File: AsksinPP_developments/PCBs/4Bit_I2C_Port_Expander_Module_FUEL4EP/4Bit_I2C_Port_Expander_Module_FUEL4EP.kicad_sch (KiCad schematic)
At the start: 22 parts, among them J1 Conn_01x04, J2 Conn_01x04, J3 Conn_01x04, J4 Conn_01x04, Q1 2N7000, Q2 2N7000, Q3 2N7000, Q4 2N7000, U1 PCA9536D

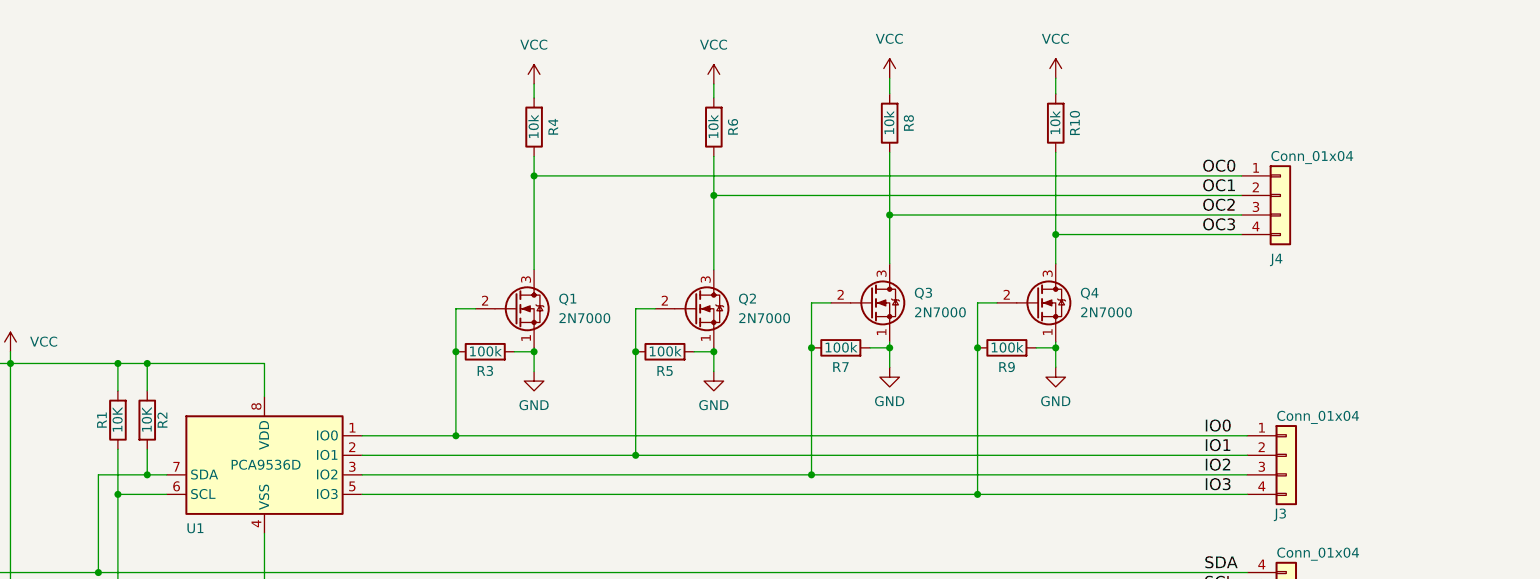
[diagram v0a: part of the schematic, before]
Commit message: PCB: I2C_Module_SHT85_BME280_FUEL4EP, I2C_Module_BME680_FUEL4EP: correction of connector placements in 3D view; 4Bit_I2C_Port_Expander_Module_FUEL4EP: change from 2N7000 to 2N7002K for SMD assembly
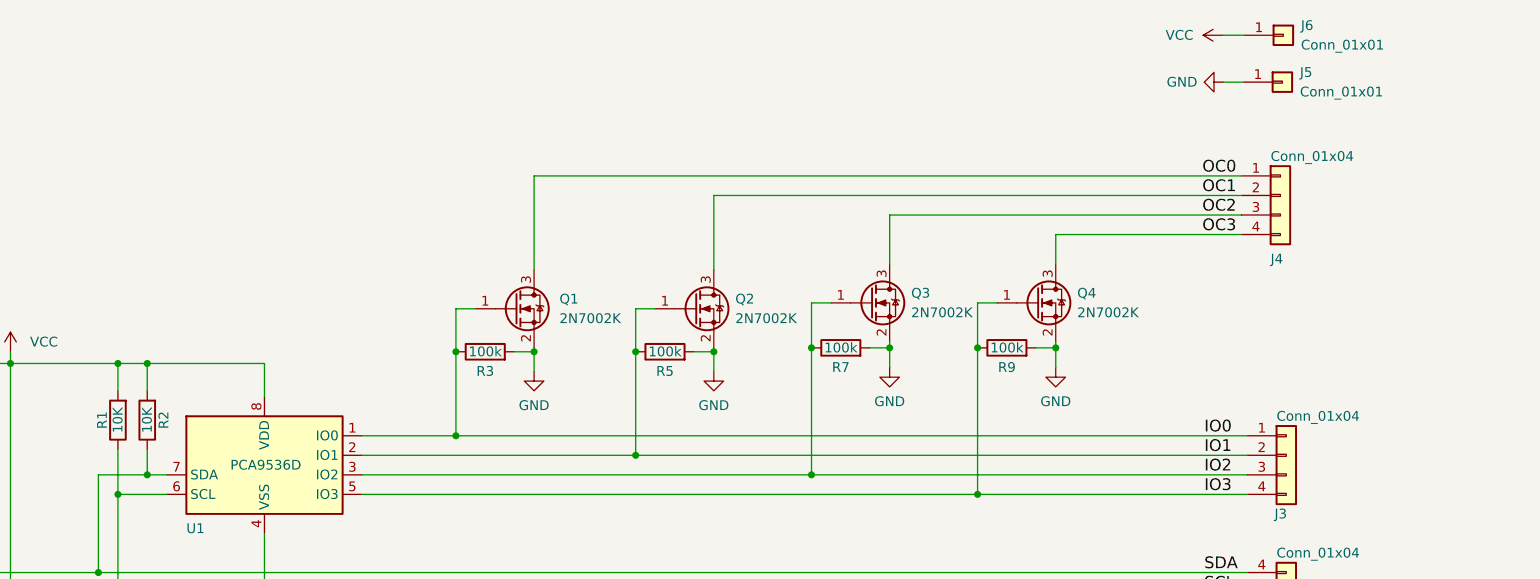
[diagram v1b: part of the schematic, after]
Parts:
- removed Q1, Q2, Q3, Q4: 2N7000, Package_TO_SOT_THT:TO-92_Inline, symbol Transistor_FET:2N7000
- removed R10, R4, R6, R8: 10k, Resistor_SMD:R_0402_1005Metric, symbol Device:R
- added J5, J6: Conn_01x01, TestPoint:TestPoint_THTPad_D1.0mm_Drill0.5mm, symbol Connector_Generic:Conn_01x01
- added Q1, Q2, Q3, Q4: 2N7002K, FUEL4EP:SOT-23_2N7002K, symbol Transistor_FET:2N7002K
- C1: LCSC (none) -> C15849; TYPE (none) -> 0603
- C2: LCSC (none) -> C1525; TYPE (none) -> 0402
- R1, R2: LCSC (none) -> C25744; TYPE (none) -> 0402
- R3, R5, R7, R9: LCSC (none) -> C25741; TYPE (none) -> 0402
- U1: LCSC (none) -> C129522; TYPE (none) -> SOIC-8
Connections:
- net GND: now also J5.1 (Pin_1), Q1.2 (S), Q2.2 (S), Q3.2 (S), Q4.2 (S)
- net IO0: now also Q1.1 (G)
- net IO1: now also Q2.1 (G)
- net IO2: now also Q3.1 (G)
- net IO3: now also Q4.1 (G)
- net OC0: now also Q1.3 (D)
- net OC1: now also Q2.3 (D)
- net OC2: now also Q3.3 (D)
- net OC3: now also Q4.3 (D)
- net SDA: now also R2.1; no longer R2.2
- net VCC: now also R2.2, J6.1 (Pin_1); no longer R2.1

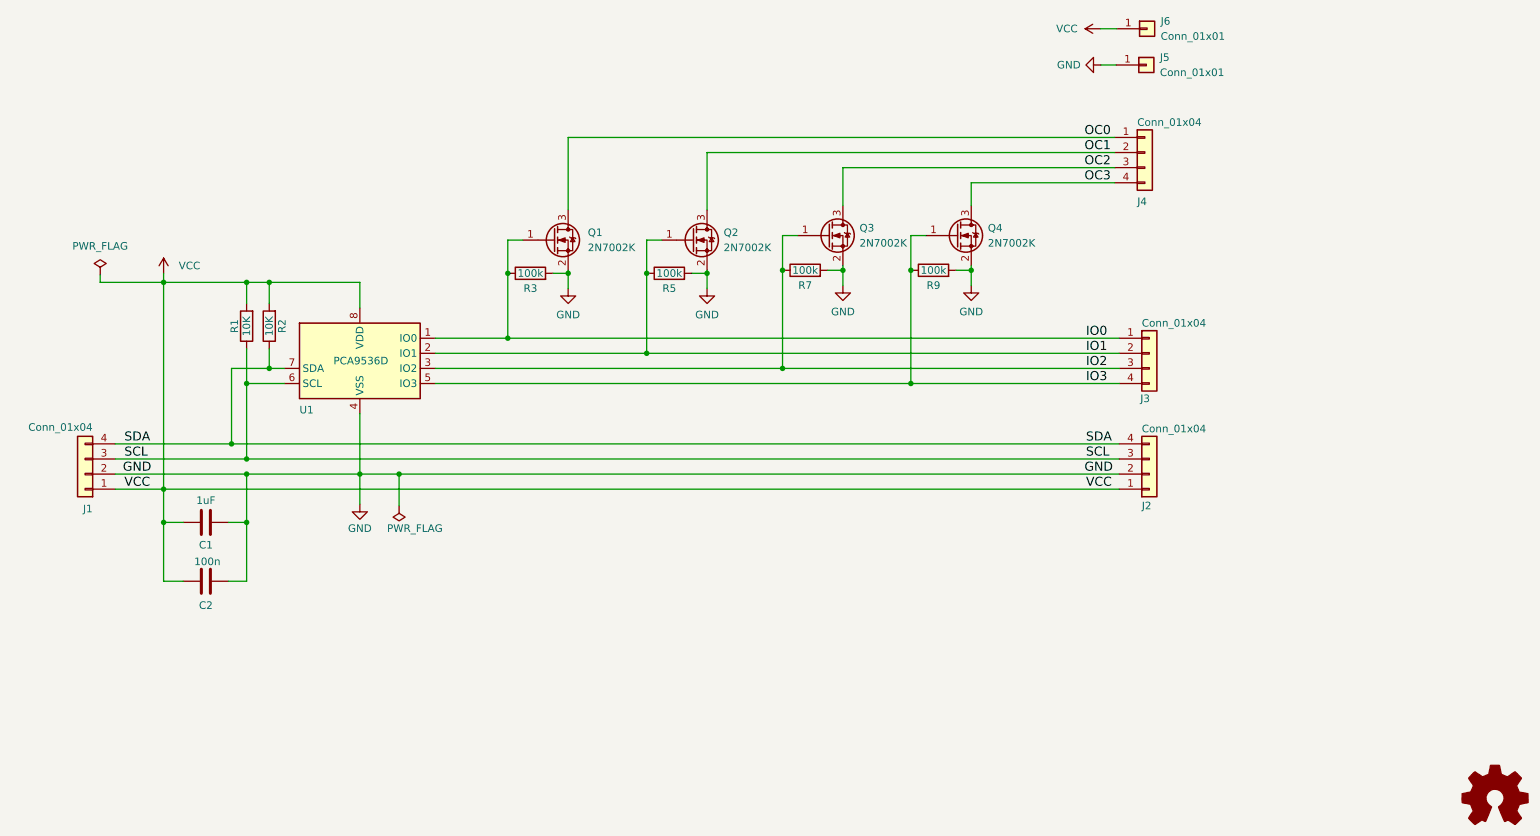
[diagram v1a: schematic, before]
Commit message: PCBs/4Bit_I2C_Port_Expander_Module_FUEL4EP: migration to KiCAD 8
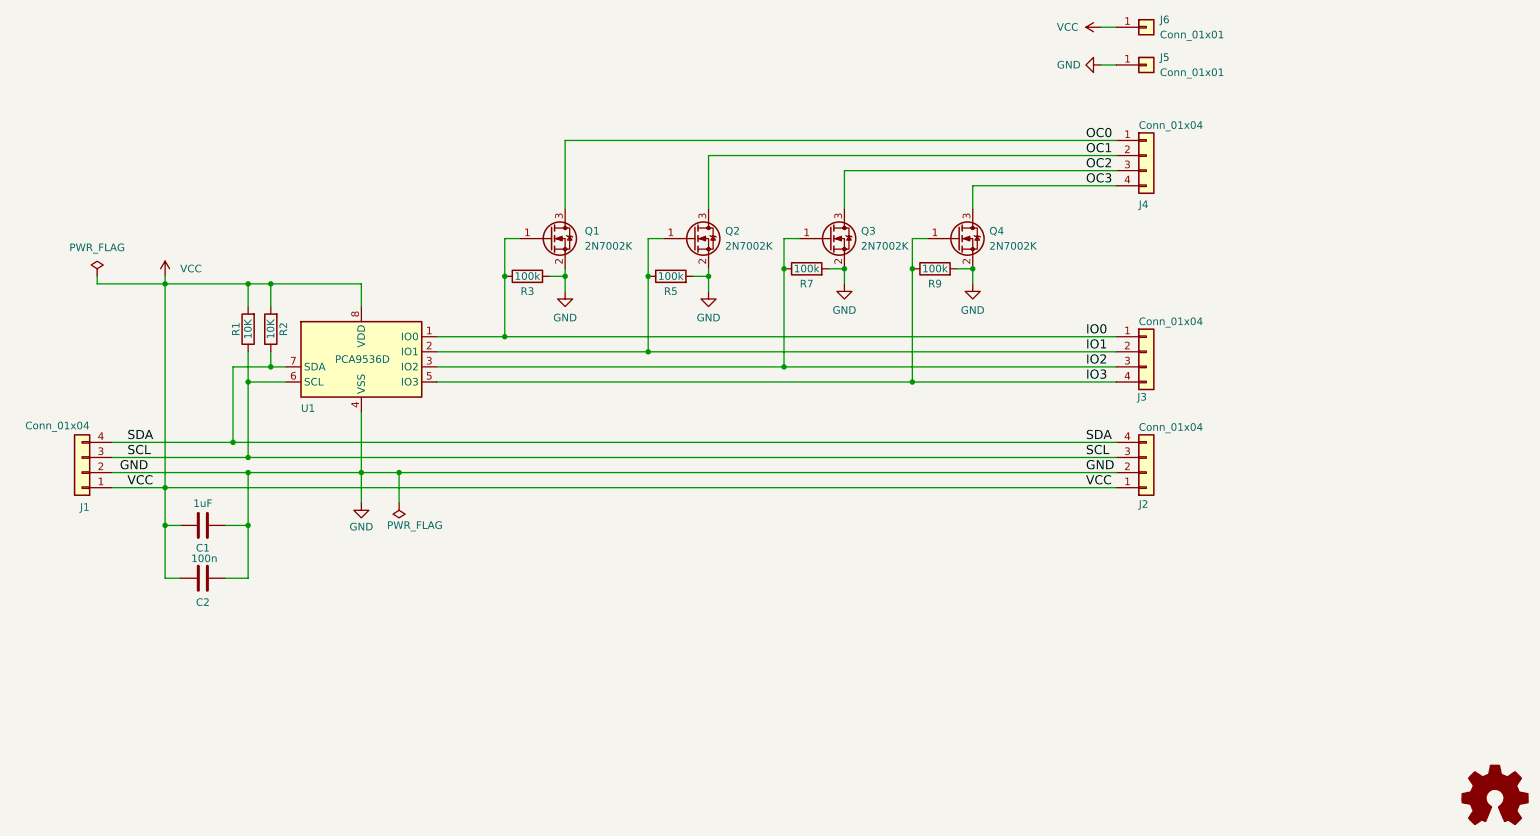
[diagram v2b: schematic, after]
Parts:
- Q1, Q2, Q3, Q4: footprint FUEL4EP:SOT-23_2N7002K -> Package_TO_SOT_SMD:SOT-23
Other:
- moved on the sheet: C1, C2, J1, J2, J3, J4, Q1, Q3, Q4, R1, R2, R3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
